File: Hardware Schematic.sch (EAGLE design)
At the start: 65 parts, among them IC1 7805T, J2 DCJ0202, J3 213598-2, T1 TIP32, T10 2N3904, T11 2N3904, T12 2N3904, T13 2N3904, T14 BD244, T15 2N3904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

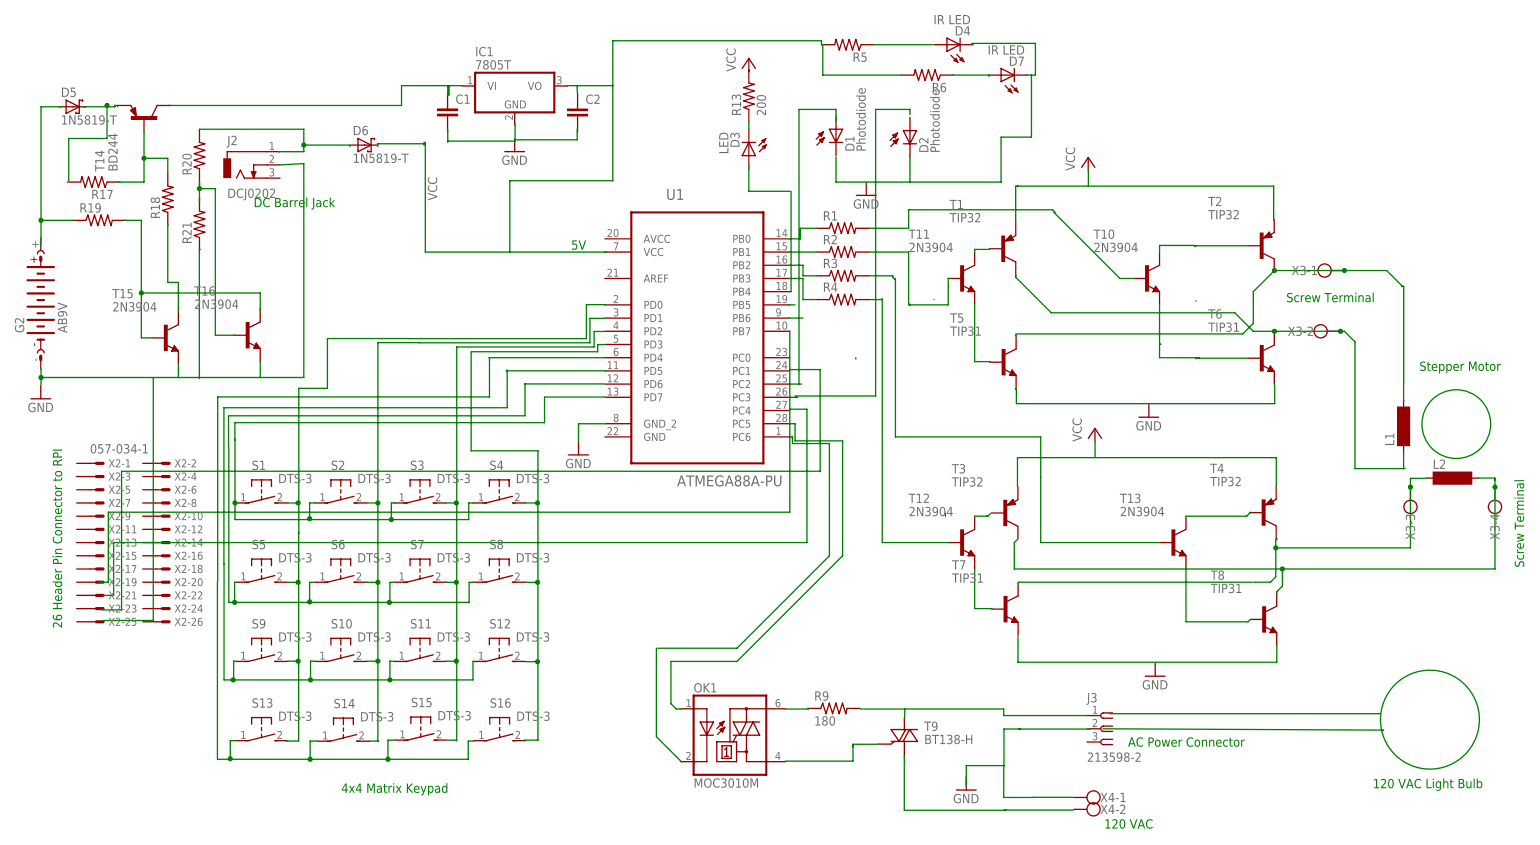
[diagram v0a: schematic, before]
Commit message: fixed stuff grounds still need to be fixed seperating the 120VAC and the other ground
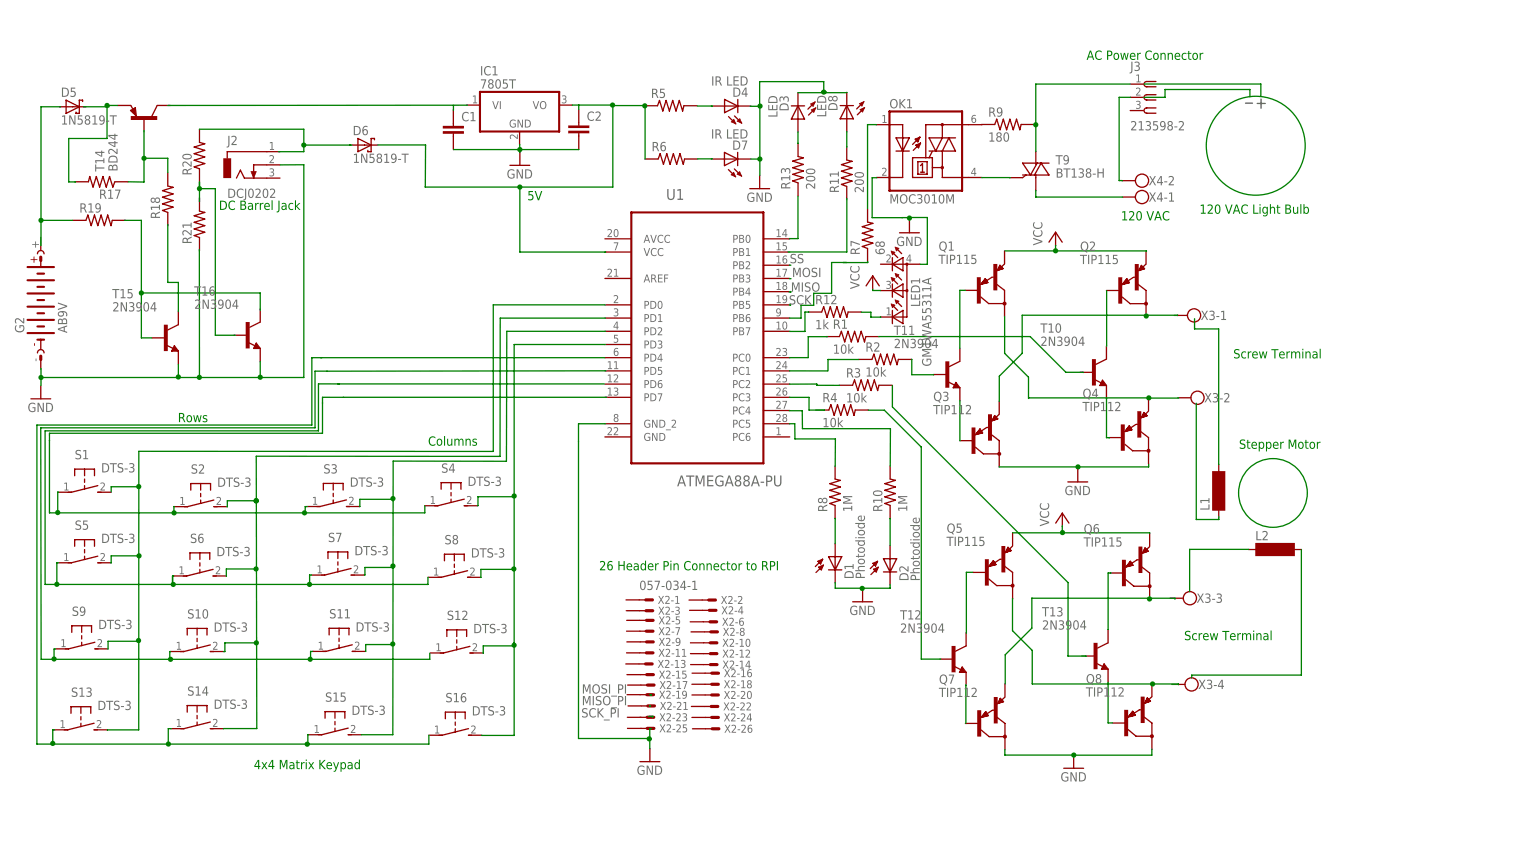
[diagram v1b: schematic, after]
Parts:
- removed T1, T2, T3, T4: TIP32, transistor:TIP32
- removed T5, T6, T7, T8: TIP31, transistor:TIP31
- added D8: LED, led:SFH482
- added LED1: GM1WA55311A, led:GM1WA55311A
- added Q1, Q2, Q5, Q6: TIP115, transistor-pnp:TIP125
- added Q3, Q4, Q7, Q8: TIP112, transistor-pnp:TIP125
- added R10, R8: 1M, rcl:R-US_0309/V
- added R11: 200, rcl:R-US_0309/V
- added R12: 1k, rcl:R-US_0309/V
- added R7: 68, rcl:R-US_0309/12
- R1, R2, R3, R4: value (none) -> 10k
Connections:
- removed net 14: R1.2
- removed net N$10: T13.C
- removed net N$13: R2.2, T11.B
- removed net N$15: T13.E
- removed net N$16: T12.C
- removed net N$17: T12.E
- removed net N$19: T11.C
- removed net N$21: T10.C
- removed net N$23: R4.2
- removed net N$25: R1.1, U1.PB0
- removed net N$26: R2.1, U1.PB1
- removed net N$27: R4.1, U1.PB3
- removed net N$28: R3.1, U1.PB2
- removed net N$30: R3.2, T13.B
- removed net N$5: X3-3.KL
- removed net N$65: J3.1
- removed net N$69: U1.PC5
- removed net N$70: U1.PC6
- removed net N$74: X3-1.KL
- removed net N$76: T12.B
- removed net N$78: T10.E
- removed net N$79: T11.E
- removed net N$8: R5.1
- removed net N$80: X3-2.KL
- removed net N$82: T10.B
- removed net N$83: U1.PC2
- removed net N$85: X3-4.KL
- removed net N$86: U1.PC3
- removed net N$88: U1.PB4
- removed net N$90: R5.2, R6.2
- removed net N$94: D3.C, R13.1
- new net N$44: S16.1
- net N$105: now also R17.1
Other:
- note added: "Columns"
- note added: "Rows"
- moved on the sheet: C1, C2, D1, D2, D3, D4, D7, IC1, J3, L1, L2, OK1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

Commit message: updated
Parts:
- added R14: 1k, rcl:R-US_0309/V
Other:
- moved on the sheet: LED1, R12
